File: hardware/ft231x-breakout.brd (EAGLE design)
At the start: 26.7 x 15.2 mm, 27 parts, among them Q1 2N7002PW, U1 FT231XS

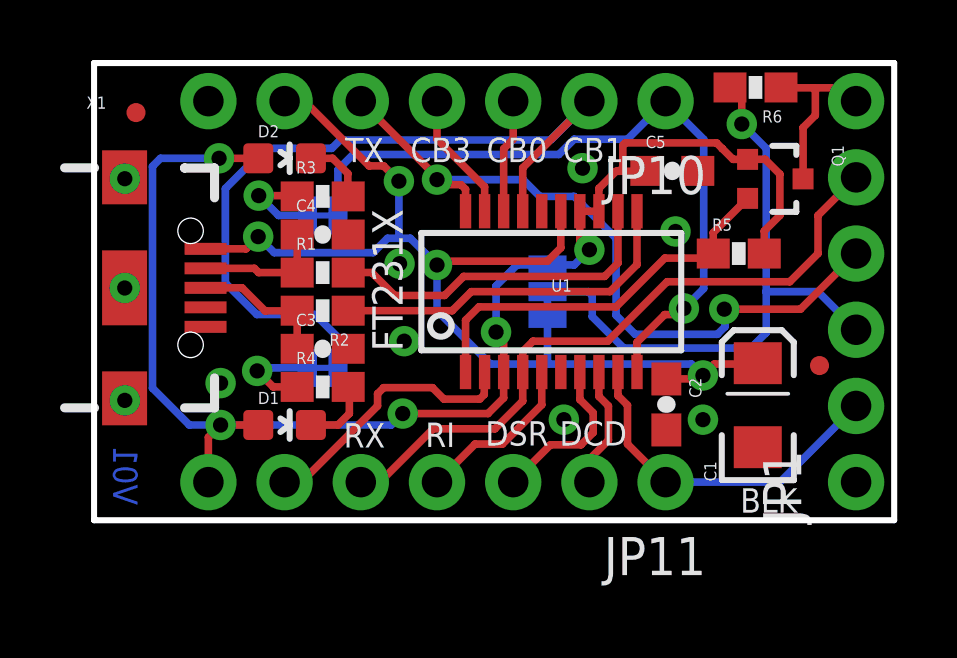
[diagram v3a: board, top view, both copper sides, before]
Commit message: Adding sch notes, small silk edits, small trace fix
Adding notes for VIN and jumper usage. Also made some small silk edits
to avoid silk getting cut off by vias. Had to make one small trace
change on 3.3V net to avoid natural bridge between pads 13 and 14.
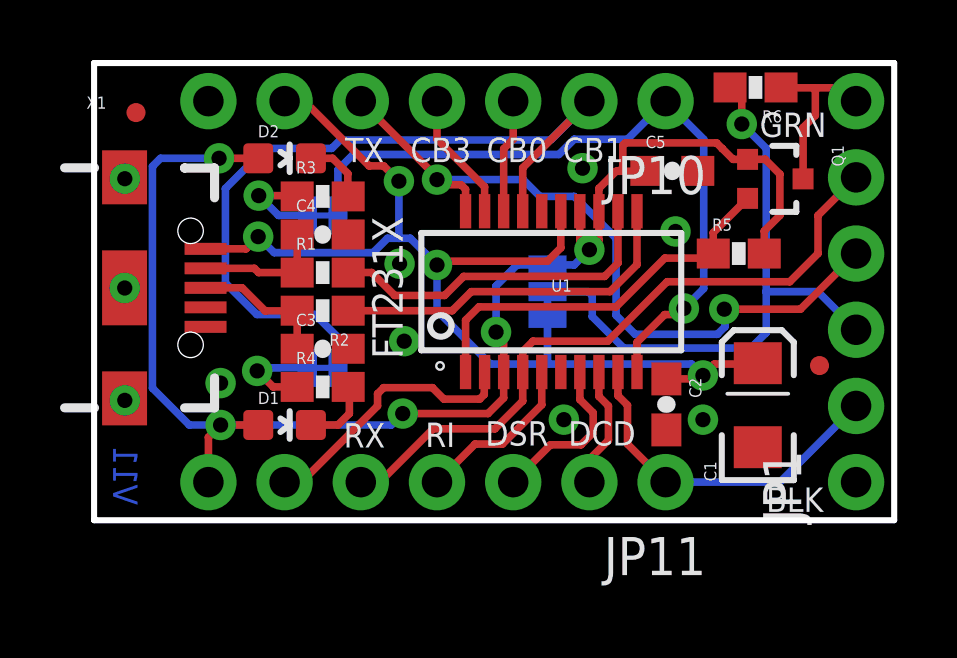
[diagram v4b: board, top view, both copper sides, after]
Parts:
- moved U$1 0.38 mm to (19.7, 7.49)
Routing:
- net 3.3V: track 48.5 -> 49.3 mm
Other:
- board text added: "GRN"
- board text added: "V11"
- board text removed: "V01"
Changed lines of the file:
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@@
 <setting verticaltext="up"/>
 </settings>
-<grid distance="0.05" unitdist="inch" unit="inch" style="lines" multiple="1" display="yes" altdistance="0.00001" altunitdist="inch" altunit="inch"/>
+<grid distance="0.05" unitdist="inch" unit="inch" style="lines" multiple="1" display="yes" altdistance="0.0005" altunitdist="inch" altunit="inch"/>
 <layers>
 <layer number="1" name="Top" color="4" fill="1" visible="yes" active="yes"/>
@@
 <layer number="39" name="tKeepout" color="4" fill="11" visible="no" active="yes"/>
 <layer number="40" name="bKeepout" color="1" fill="11" visible="no" active="yes"/>
-<layer number="41" name="tRestrict" color="4" fill="10" visible="no" active="yes"/>
+<layer number="41" name="tRestrict" color="4" fill="10" visible="yes" active="yes"/>
 <layer number="42" name="bRestrict" color="1" fill="10" visible="no" active="yes"/>
 <layer number="43" name="vRestrict" color="2" fill="10" visible="no" active="yes"/>
@@
 <layer number="45" name="Holes" color="7" fill="1" visible="yes" active="yes"/>
 <layer number="46" name="Milling" color="3" fill="1" visible="no" active="yes"/>
-<layer number="47" name="Measures" color="7" fill="1" visible="yes" active="yes"/>
+<layer number="47" name="Measures" color="7" fill="1" visible="no" active="yes"/>
 <layer number="48" name="Document" color="7" fill="1" visible="no" active="yes"/>
 <layer number="49" name="Reference" color="7" fill="1" visible="yes" active="yes"/>
@@
 <text x="3.556" y="2.54" size="0.8128" layer="22" font="vector" ratio="15" rot="MR90" align="center-left">3.3</text>
 <text x="3.81" y="12.7" size="0.8128" layer="22" font="vector" ratio="15" rot="MR90" align="center-right">GND</text>
-<text x="23.4442" y="0.6604" size="0.8128" layer="21" font="vector" ratio="15" align="center-right">BLK</text>
+<text x="24.3078" y="0.6858" size="0.8128" layer="21" font="vector" ratio="15" align="center-right">BLK</text>
 <text x="11.557" y="11.938" size="0.8128" layer="21" font="vector" ratio="15" rot="R180" align="top-center">CB3</text>
 <text x="14.097" y="11.938" size="0.8128" layer="21" font="vector" ratio="15" rot="R180" align="top-center">CB0</text>
 <text x="16.637" y="11.938" size="0.8128" layer="21" font="vector" ratio="15" rot="R180" align="top-center">CB1</text>
 <text x="9.017" y="11.938" size="0.8128" layer="21" font="vector" ratio="15" rot="R180" align="top-center">TX</text>
-<text x="16.637" y="3.302" size="0.8128" layer="21" font="vector" ratio="15" rot="R180" align="bottom-center">DCD</text>
+<text x="16.9291" y="3.302" size="0.8128" layer="21" font="vector" ratio="15" rot="R180" align="bottom-center">DCD</text>
 <text x="14.097" y="3.302" size="0.8128" layer="21" font="vector" ratio="15" rot="R180" align="bottom-center">DSR</text>
 <text x="11.53668125" y="3.256278125" size="0.8128" layer="21" font="vector" ratio="15" rot="R180" align="bottom-center">RI</text>
 <text x="9.00938125" y="3.235959375" size="0.8128" layer="21" font="vector" ratio="15" rot="R180" align="bottom-center">RX</text>
-<text x="9.271" y="8.001" size="1.016" layer="21" font="vector" ratio="15" rot="R90" align="top-center">FT231X</text>
+<text x="9.271" y="7.747" size="1.016" layer="21" font="vector" ratio="15" rot="R90" align="top-center">FT231X</text>
 <text x="15.113" y="5.969" size="0.8128" layer="22" font="vector" ratio="15" rot="MR0" align="top-center">5V</text>
 <text x="14.986" y="9.271" size="0.8128" layer="22" font="vector" ratio="15" rot="MR180" align="top-center">3.3</text>
@@
 <text x="14.859" y="-11.43" size="1.6764" layer="51" font="vector" ratio="12">J. Lindblom</text>
 <text x="0.381" y="-13.97" size="1.6764" layer="51" font="vector" ratio="12">Revised by: Patrick Alberts</text>
-<text x="0.635" y="0.508" size="0.8128" layer="16" font="vector" ratio="12" rot="MR90">V01</text>
+<text x="0.635" y="0.508" size="0.8128" layer="16" font="vector" ratio="12" rot="MR90">V11</text>
+<text x="24.4094" y="13.1826" size="0.8128" layer="21" font="vector" ratio="15" align="center-right">GRN</text>
+<circle x="11.5316" y="5.1435" radius="0.0381" width="0.254" layer="21"/>
 </plain>
 <attributes>
@@
 <attribute name="VALUE" value="10K" x="22.0472" y="14.4272" size="1.778" layer="27" rot="R180" display="off"/>
 </element>
-<element name="U$1" library="SparkFun-Aesthetics" package="OSHW-LOGO-S" value="OSHW-LOGOS" x="19.304" y="7.493" smashed="yes" rot="MR0"/>
+<element name="U$1" library="SparkFun-Aesthetics" package="OSHW-LOGO-S" value="OSHW-LOGOS" x="19.685" y="7.493" smashed="yes" rot="MR0"/>
 <element name="JP3" library="SparkFun-Aesthetics" package="MICRO-FIDUCIAL" value="FIDUCIALUFIDUCIAL" x="1.397" y="13.589"/>
 <element name="JP4" library="SparkFun-Aesthetics" package="MICRO-FIDUCIAL" value="FIDUCIALUFIDUCIAL" x="24.1808" y="5.1562"/>
@@
 <contactref element="U1" pad="14"/>
 <contactref element="SJ1" pad="1"/>
-<wire x1="16.8275" y1="10.2997" x2="16.1925" y2="10.2997" width="0.254" layer="1"/>
 <via x="16.51" y="9.017" extent="1-16" drill="0.508"/>
 <wire x1="16.1925" y1="10.2997" x2="16.1925" y2="9.3345" width="0.254" layer="1"/>
@@
 <wire x1="9.906" y1="3.175" x2="4.2164" y2="3.175" width="0.254" layer="16"/>
 <wire x1="16.8275" y1="10.2997" x2="16.8275" y2="11.0617" width="0.254" layer="1"/>
-<wire x1="16.8275" y1="11.0617" x2="17.399" y2="11.6332" width="0.254" layer="1"/>
 <wire x1="4.2164" y1="3.175" x2="3.175" y2="3.175" width="0.254" layer="16"/>
 <wire x1="9.906" y1="3.175" x2="10.287" y2="3.556" width="0.254" layer="16"/>
@@
 <wire x1="22.86" y1="10.16" x2="22.86" y2="11.53668125" width="0.254" layer="1"/>
 <wire x1="22.86" y1="11.53668125" x2="22.3647" y2="12.03198125" width="0.254" layer="1"/>
-<wire x1="17.399" y1="11.6332" x2="17.50568125" y2="11.6332" width="0.254" layer="1"/>
-<wire x1="17.50568125" y1="11.6332" x2="18.410821875" y2="11.6332" width="0.254" layer="1"/>
 <wire x1="18.410821875" y1="11.6332" x2="18.423521875" y2="11.6459" width="0.254" layer="1"/>
 <wire x1="22.3647" y1="12.03198125" x2="21.78538125" y2="12.03198125" width="0.254" layer="1"/>
@@
 <wire x1="17.625059375" y1="12.4968" x2="17.625059375" y2="11.752578125" width="0.254" layer="1"/>
 <wire x1="17.625059375" y1="11.752578125" x2="17.50568125" y2="11.6332" width="0.254" layer="1"/>
+<wire x1="16.8275" y1="10.2997" x2="16.8275" y2="9.3345" width="0.254" layer="1"/>
+<wire x1="16.8275" y1="9.3345" x2="16.51" y2="9.017" width="0.254" layer="1"/>
+<wire x1="16.8275" y1="11.0617" x2="17.399" y2="11.6332" width="0.254" layer="1"/>
+<wire x1="17.399" y1="11.6332" x2="17.50568125" y2="11.6332" width="0.254" layer="1"/>
+<wire x1="17.50568125" y1="11.6332" x2="18.410821875" y2="11.6332" width="0.254" layer="1"/>
 </signal>
 <signal name="CBUS3">

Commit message: Via drills change, moved R6 and library package update
Dropped all vias excepting the 3 usb connector staking vias to 15 mil to
jive better with silk. Moved R6 further in from edge of board to avoid
DPN damage/danger. Ran library update to include polarity mark silk
edits to SSOP20 package. Bumped micro-fiducials up to full fiducial
size.
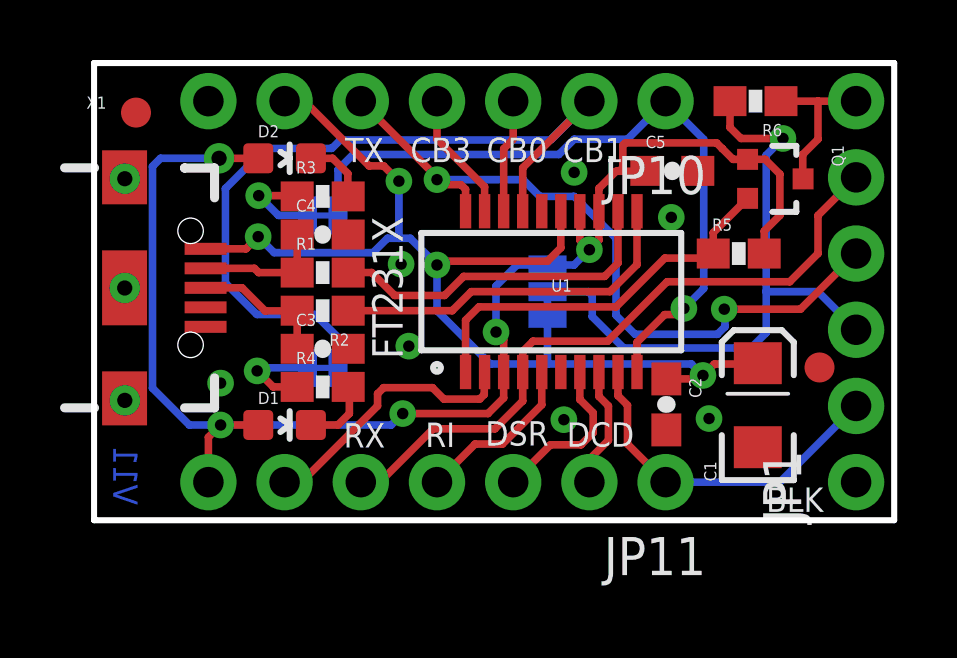
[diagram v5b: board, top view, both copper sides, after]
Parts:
- JP3, JP4: value FIDUCIALUFIDUCIAL -> FIDUCIAL1X2; device SparkFun-Aesthetics:MICRO-FIDUCIAL -> SparkFun-Aesthetics:FIDUCIAL-1X2
- U1: value FT231XS -> FTS31XS-U
- moved R6 0.46 mm to (22.0, 14.0)
- moved JP4 0.06 mm to (24.2, 5.09)
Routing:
- net VOUT: track 20.9 -> 21.7 mm
- net RESET: track 5.94 -> 5.31 mm
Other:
- board text removed: "GRN"

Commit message: Fixing issues from design checklist
See issue #4 in repo for full rundown.
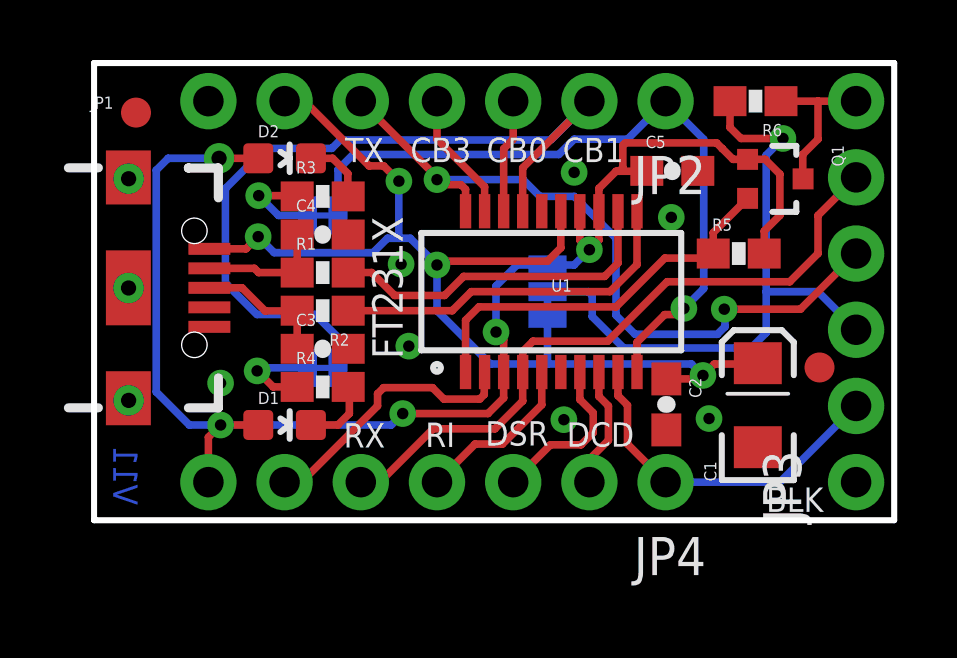
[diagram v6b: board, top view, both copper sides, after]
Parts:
- removed JP11: (no value), SparkFun-Connectors:1X07_NS
- removed X1: (no value), SparkFun-Connectors:USB-AB-MICRO-SMD_V03
- added JP5, JP6: FIDUCIAL1X2, SparkFun-Aesthetics:FIDUCIAL-1X2
- JP1: device SparkFun-Connectors:1X06_NS -> SparkFun-Connectors:USB-AB-MICRO-SMD_V03
- JP3: value FIDUCIAL1X2 -> (none); device SparkFun-Aesthetics:FIDUCIAL-1X2 -> SparkFun-Connectors:1X06_NS
- JP4: value FIDUCIAL1X2 -> (none); device SparkFun-Aesthetics:FIDUCIAL-1X2 -> SparkFun-Connectors:1X07_NS
- moved JP3 27.0 mm to (25.4, 1.27), turned to 90 degrees
- moved JP1 25.1 mm to (1.14, 7.75), turned to 0 degrees
- moved JP4 6.40 mm to (19.1, 1.27), turned to 180 degrees
- renumbered JP10 to JP2
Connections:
- net 3.3V: now also JP4.7; no longer JP11.7
- net CTS: now also JP3.2, JP4.1; no longer JP1.2, JP11.1
- net DCD: now also JP4.2; no longer JP11.2
- net DSR: now also JP4.3; no longer JP11.3
- net GND: now also JP1.GND1, JP1.SHIELD1, JP1.SHIELD2, JP1.SHIELD3, JP3.1; no longer JP1.1, X1.GND1
- net N$3: now also JP1.D+1; no longer X1.D+1
- net N$4: now also JP1.D-1; no longer X1.D-1
- net RESET: now also JP3.6; no longer JP1.6
- net RI: now also JP4.4; no longer JP11.4
- net RTS: now also JP4.6; no longer JP11.6
- net RXD: now also JP3.5, JP4.5; no longer JP1.5, JP11.5
- net TXD: now also JP3.4; no longer JP1.4
- net VCC: now also JP1.VBUS1; no longer X1.VBUS1
- net VOUT: now also JP3.3; no longer JP1.3
